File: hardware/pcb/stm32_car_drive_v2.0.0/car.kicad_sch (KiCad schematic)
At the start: 41 parts, among them J0 OLED, J14 OLED, J15 Conn_01x02, J17 Conn_01x05, J18 Conn_01x02, J19 Conn_01x02, J20 Conn_01x09, J22 Conn_01x10, J24 Conn_01x02, J25 HC-05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

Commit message: update
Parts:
- removed D6, D7: LED, LED_SMD:LED_0805_2012Metric, symbol Library:LED
- removed HC-SR04: HC-SR04, Connector_PinSocket_2.54mm:PinSocket_1x04_P2.54mm_Vertical, symbol Library:Conn_01x04
- removed J0, J14: OLED, Connector_PinSocket_2.54mm:PinSocket_1x04_P2.54mm_Vertical, symbol Library:Conn_01x04
- removed J15: Conn_01x02, myself:HDR-TH_2P-P2.00-V-F-1, symbol Library:Conn_01x02
- removed J17: Conn_01x05, Connector_PinSocket_2.54mm:PinSocket_1x05_P2.54mm_Vertical, symbol Library:Conn_01x05
- removed J19, J24: Conn_01x02, Connector_PinSocket_2.54mm:PinSocket_1x02_P2.54mm_Vertical, symbol Library:Conn_01x02
- removed J20: Conn_01x09, Connector_PinSocket_2.54mm:PinSocket_1x09_P2.54mm_Vertical, symbol Library:Conn_01x09
- removed J25: HC-05, Connector_PinSocket_2.54mm:PinSocket_1x06_P2.54mm_Vertical, symbol Library:Conn_01x06
- removed J26: Conn_01x08, Connector_PinHeader_2.54mm:PinHeader_1x06_P2.54mm_Vertical, symbol Library:Conn_01x08
- removed R10, R11: 10k, Resistor_SMD:R_0603_1608Metric, symbol Library:R_Small
- removed SW4: K6, DuRuofu_Switch:SW_Push_1P1T_NO_6x6mm, symbol Library:SW_Push
- removed SW5: K5, DuRuofu_Switch:SW_Push_1P1T_NO_6x6mm, symbol Library:SW_Push
- added J10, J12, J5, J6: Conn_01x02, Connector_PinHeader_2.54mm:PinHeader_1x02_P2.54mm_Vertical, symbol Library:Conn_01x02
- added J14, J15, J17, J21: Conn_01x03, Connector_PinHeader_2.54mm:PinHeader_1x03_P2.54mm_Vertical, symbol Connector_Generic:Conn_01x03
- added J16: HC-05, Connector_PinSocket_2.54mm:PinSocket_1x06_P2.54mm_Vertical, symbol Library:Conn_01x06
- added J19: Conn_01x08, DuRuofu_Module:MPU6050-GY-521, symbol Library:Conn_01x08
- added J20: Conn_02x08_Counter_Clockwise, Connector_PinHeader_2.54mm:PinHeader_2x08_P2.54mm_Vertical, symbol Connector_Generic:Conn_02x08_Counter_Clockwise
- added OLED1: OLED_0.96, DuRuofu_Module:0.96OLED_4P, symbol DuRuofu_Module:0.96OLED_4P
- added R3, R4: 0, Resistor_SMD:R_0603_1608Metric, symbol Library:R
- J18: footprint Connector_PinSocket_2.54mm:PinSocket_1x02_P2.54mm_Vertical -> Connector_PinHeader_2.54mm:PinHeader_1x02_P2.54mm_Vertical
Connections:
- net +3.3V: now also J16.2 (Pin_2), J19.1 (Pin_1), J20.16 (Pin_16), OLED1.2 (VCC)
- net +5V: now also J14.2 (Pin_2), J15.2 (Pin_2), J17.2 (Pin_2), J21.2 (Pin_2)
- net GND: now also J14.3 (Pin_3), J15.3 (Pin_3), J16.1 (Pin_1), J17.3 (Pin_3), J19.2 (Pin_2), J20.14 (Pin_14), J20.15 (Pin_15), J21.3 (Pin_3), OLED1.1 (GND)
- net PA10 renamed KEY1
- net PA11: no longer names the net of U10.2 (TXD)
- net PA11: now also R3.2; no longer SW2.1
- net PA12: no longer names the net of U10.3 (RXD)
- net PA12: now also R4.2; no longer SW3.1
- net PA2 renamed USART2_TX
- net USART2_TX: now also J5.1 (Pin_1)
- net PA3 renamed USART2_RX
- net USART2_RX: now also J5.2 (Pin_2)
- net PA8 renamed LED1
- net PB10 renamed USART3_TX
- net USART3_TX: now also J6.1 (Pin_1)
- net PB11 renamed USART3_RX
- net USART3_RX: now also J6.2 (Pin_2)
- net PB12 renamed Buzzer
- net PB15 renamed KEY4
- net PB3 renamed LED2
- net PB6 renamed USART1_TX
- net USART1_TX: now also R3.1
- net PB7 renamed USART1_RX
- net USART1_RX: now also R4.1
- net PD2 renamed LED3
- new net -PB2: J20.1 (Pin_1)
- new net -PB3: J20.2 (Pin_2)
- new net -PC0: J20.3 (Pin_3)
- new net -PC1: J20.4 (Pin_4)
- new net -PC13: J20.11 (Pin_11)
- new net -PC14: J20.12 (Pin_12)
- new net -PC15: J20.13 (Pin_13)
- new net -PC2: J20.5 (Pin_5)
- new net -PC3: J20.6 (Pin_6)
- new net -PC4: J20.7 (Pin_7)
- new net -PC5: J20.8 (Pin_8)
- new net -PC8: J20.9 (Pin_9)
- new net -PC9: J20.10 (Pin_10)
- new net KEY2: SW2.1
- new net KEY3: SW3.1
- new net MPU_SCL: J19.3 (Pin_3)
- new net MPU_SDA: J19.4 (Pin_4)
- new net OLED_ACL: OLED1.3 (SCL)
- new net OLED_SDA: OLED1.4 (SDA)
- new net TIM3_CH1: J14.1 (Pin_1)
- new net TIM3_CH2: J15.1 (Pin_1)
- new net TIM3_CH3: J17.1 (Pin_1)
- new net TIM3_CH4: J21.1 (Pin_1)
- new net USART4_RX: J10.2 (Pin_2), J16.4 (Pin_4)
- new net USART4_TX: J10.1 (Pin_1), J16.3 (Pin_3)
- new net USART5_RX: J12.2 (Pin_2)
- new net USART5_TX: J12.1 (Pin_1)
- no-connect marks 13 -> 15
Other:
- note added: "Expansion interface"
- note added: "HC-05 Bluetooth module"
- note added: "Indicator Buzzer"
- note added: "Servo motor"
- note added: "TOF25 USART4"
- note added: "USART4"
- note added: "USART5"
- note added: "Use software simulation I2C"
- note added: "button * 4"
- note removed: "ADC"
- note removed: "Button * 6"
- note removed: "HC-05蓝牙模块"
- note removed: "I2C"
- note removed: "TOF250"
- note removed: "多余接口"
- note removed: "舵机驱动"
- note removed: "超声波测距"
- moved on the sheet: BZ2, C10, C3, D2, D3, D4, D5, J18, J22, J3, K210, P1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

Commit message: feat(pcb): 更新PCB封装
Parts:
- removed J22: Conn_01x10, Connector_JST:JST_XH_B8B-XH-A_1x08_P2.50mm_Vertical, symbol Library:Conn_01x10
- added J24: Conn_01x04, Connector_PinSocket_2.54mm:PinSocket_1x04_P2.54mm_Vertical, symbol Library:Conn_01x04
- J14, J15, J17, J21: symbol Connector_Generic:Conn_01x03 -> Library:Conn_01x03
- J19: footprint DuRuofu_Module:MPU6050-GY-521 -> Library:MPU6050-GY-521
- J20: symbol Connector_Generic:Conn_02x08_Counter_Clockwise -> Library:Conn_02x08_Counter_Clockwise
- OLED1: footprint DuRuofu_Module:0.96OLED_4P -> Library:0.96OLED_4P; symbol DuRuofu_Module:0.96OLED_4P -> Library:0.96OLED_4P
- P1: footprint Connector_USB:USB_C_Receptacle_GCT_USB4105-xx-A_16P_TopMnt_Horizontal -> Library:USB_C_Receptacle_GCT_USB4105-xx-A_16P_TopMnt_Horizontal
- SW1, SW2, SW3, SW6: footprint DuRuofu_Switch:SW_Push_1P1T_NO_6x6mm -> Library:SW_Push_1P1T_NO_6x6mm
- U10: footprint Package_SO:SOIC-16_3.9x9.9mm_P1.27mm -> Library:SOIC-16_3.9x9.9mm_P1.27mm
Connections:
- net +5V: now also J24.1 (Pin_1)
- net -PB2: now also J24.3 (Pin_3)
- net -PB3: now also J24.4 (Pin_4)
- net GND: now also J24.2 (Pin_2)
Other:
- note added: "Eight-way grayscale sensor"
- note removed: "八路灰度传感器"

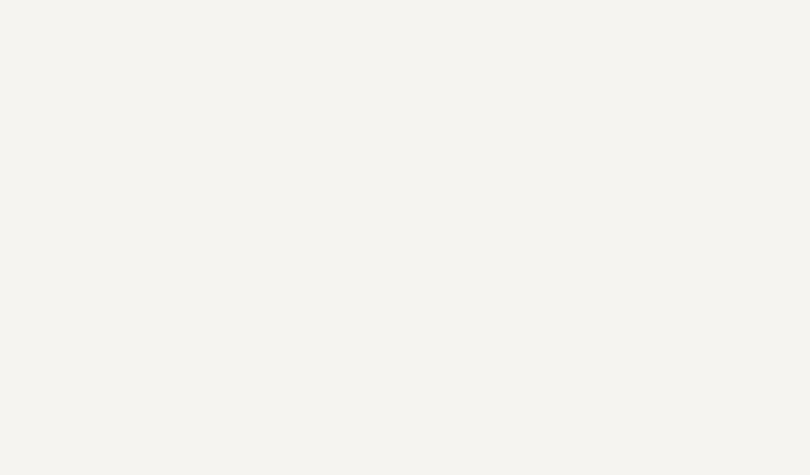
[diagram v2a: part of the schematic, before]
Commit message: feat(pcb):更新布局
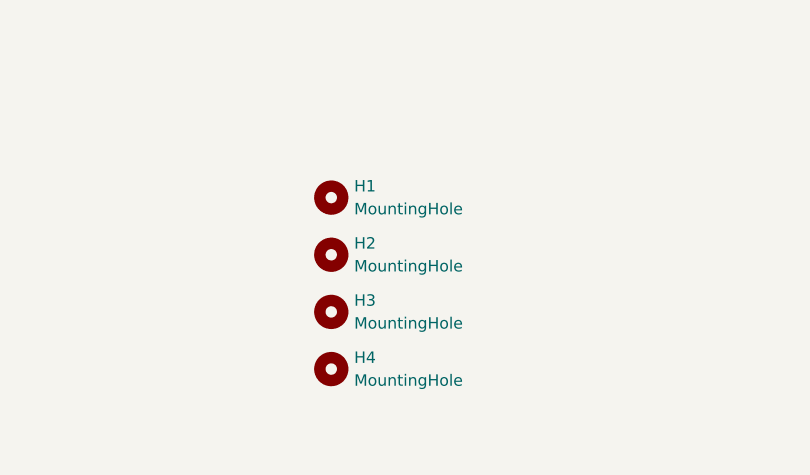
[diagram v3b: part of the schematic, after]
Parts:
- added H1, H2, H3, H4: MountingHole, MountingHole:MountingHole_3.2mm_M3_DIN965_Pad, symbol Library:MountingHole
- J16: footprint Connector_PinSocket_2.54mm:PinSocket_1x06_P2.54mm_Vertical -> Connector_PinHeader_2.54mm:PinHeader_1x06_P2.54mm_Vertical
- J24: footprint Connector_PinSocket_2.54mm:PinSocket_1x04_P2.54mm_Vertical -> Connector_PinHeader_2.54mm:PinHeader_1x04_P2.54mm_Vertical

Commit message: 连线
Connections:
- net +3V3 is gone; now on net +3.3V: SW1.2, SW2.2, SW3.2, SW6.2
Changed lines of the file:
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@@
 	)
 	(junction
+		(at 189.23 142.24)
+		(diameter 0)
+		(color 0 0 0 0)
+	)
+	(junction
 		(at 116.84 142.24)
 		(diameter 0)
@@
 	)
 	(junction
-		(at 189.23 142.24)
-		(diameter 0)
-		(color 0 0 0 0)
-	)
-	(junction
 		(at 273.05 143.51)
 		(diameter 0)
@@
 	)
 	(symbol
+		(lib_id "Library:+3.3V")
+		(at 189.23 142.24 0)
+		(unit 1)
+		(exclude_from_sim no)
+		(in_bom yes)
+		(on_board yes)
+		(dnp no)
+		(property "Reference" "#PWR057"
+			(at 189.23 146.05 0)
+			(effects
+				(font
+					(size 1.27 1.27)
+				)
+				(hide yes)
+			)
+		)
+		(property "Value" "+3.3V"
+			(at 189.738 138.684 0)
+			(effects
+				(font
+					(size 1.27 1.27)
+				)
+			)
+		)
+		(property "Footprint" ""
+			(at 189.23 142.24 0)
+			(effects
+				(font
+					(size 1.27 1.27)
+				)
+				(hide yes)
+			)
+		)
+		(property "Datasheet" ""
+			(at 189.23 142.24 0)
+			(effects
+				(font
+					(size 1.27 1.27)
+				)
+				(hide yes)
+			)
+		)
+		(property "Description" "Power symbol creates a global label with name \"+3.3V\""
+			(at 189.23 142.24 0)
+			(effects
+				(font
+					(size 1.27 1.27)
+				)
+				(hide yes)
+			)
+		)
+		(pin "1"
+		)
+		(instances
+			(project "car"
+				(path "/6ff1c62f-229a-40ac-8189-775d26f32bff"
+					(reference "#PWR057")
+					(unit 1)
+				)
+			)
+		)
+	)
+	(symbol
 		(lib_id "Library:MountingHole")
 		(at 218.44 233.68 0)
@@
 					(unit 1)
 				)
-			)
-		)
-	)
-	(symbol
-		(lib_id "Library:+3V3")
-		(at 189.23 142.24 0)
-		(unit 1)
-		(exclude_from_sim no)
-		(in_bom yes)
-		(on_board yes)
-		(dnp no)
-		(fields_autoplaced yes)
-		(property "Reference" "#PWR057"
-			(at 189.23 146.05 0)
-			(effects
-				(font
-					(size 1.27 1.27)
-				)
-				(hide yes)
-			)
-		)
-		(property "Value" "+3V3"
-			(at 189.23 137.16 0)
-			(effects
-				(font
-					(size 1.27 1.27)
-				)
-			)
-		)
-		(property "Footprint" ""
-			(at 189.23 142.24 0)
-			(effects
-				(font
-					(size 1.27 1.27)
-				)
-				(hide yes)
-			)
-		)
-		(property "Datasheet" ""
-			(at 189.23 142.24 0)
-			(effects
-				(font
-					(size 1.27 1.27)
-				)
-				(hide yes)
-			)
-		)
-		(property "Description" "Power symbol creates a global label with name \"+3V3\""
-			(at 189.23 142.24 0)
-			(effects
-				(font
-					(size 1.27 1.27)
-				)
-				(hide yes)
-			)
-		)
-		(pin "1"
-		)
-		(instances
-			(project "car"
-				(path "/6ff1c62f-229a-40ac-8189-775d26f32bff"
-					(reference "#PWR057")
-					(unit 1)
-				)
